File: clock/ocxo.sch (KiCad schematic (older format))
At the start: 32 parts

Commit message: Fill in some of the BOM entries.
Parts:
- removed Q?: Q_NPN_BCE, symbol Q_NPN_BCE
- added C?: 470pF, symbol C
- added Q?: MMBT3904, symbol Q_NPN_BEC
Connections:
- wire segments 164 -> 127
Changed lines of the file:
@@
 $Descr A4 11693 8268
 encoding utf-8
-Sheet 3 5
+Sheet 2 5
 Title ""
 Date ""
@@
 $EndComp
 $Comp
-L Q_NPN_BCE Q?
-U 1 1 561CA517
-P 6050 2650
-F 0 "Q?" H 6350 2700 50  0000 R CNN
-F 1 "Q_NPN_BCE" H 6650 2600 50  0000 R CNN
-F 2 "" H 6250 2750 29  0000 C CNN
-F 3 "" H 6050 2650 60  0000 C CNN
-	1    6050 2650
-	1    0    0    -1
-$EndComp
-$Comp
 L R_local R?
 U 1 1 561CA9D0
@@
 	1650 1350 7100 1350
 Wire Wire Line
-	4950 1150 5150 1150
-Wire Wire Line
-	5150 1150 6600 1150
-Wire Wire Line
-	6600 1150 6950 1150
-Wire Wire Line
-	6950 1150 7100 1150
+	4950 1150 7100 1150
 Wire Wire Line
 	6950 1450 6950 1150
@@
 	6600 1750 6600 1950
 Wire Wire Line
-	6600 1950 6950 1950
-Wire Wire Line
-	6950 1950 7350 1950
-Wire Wire Line
-	7350 1950 7700 1950
-Wire Wire Line
-	7700 1950 8550 1950
-Wire Wire Line
-	8550 1950 8950 1950
+	6600 1950 8950 1950
 Wire Wire Line
 	6950 1950 6950 1750
@@
 	4450 1150 4650 1150
 Wire Wire Line
-	1650 1150 2850 1150
-Wire Wire Line
-	2850 1150 3900 1150
-Wire Wire Line
-	3900 1150 4150 1150
-Wire Wire Line
-	3900 1150 3900 1550
-Wire Wire Line
-	3900 1550 3900 1650
+	1650 1150 4150 1150
+Wire Wire Line
+	3900 1150 3900 1650
 Wire Wire Line
 	3900 1550 4750 1550
 Wire Wire Line
-	4750 1550 4750 1750
-Wire Wire Line
-	4750 1750 4750 1900
+	4750 1550 4750 1900
 Connection ~ 3900 1150
 Wire Wire Line
@@
 	7700 1950 7700 1650
 Wire Wire Line
-	8300 1150 8550 1150
-Wire Wire Line
-	8550 1150 8950 1150
-Wire Wire Line
-	8950 1150 9350 1150
+	8300 1150 9350 1150
 Wire Wire Line
 	8550 1450 8550 1150
@@
 	1650 1550 2250 1550
 Wire Wire Line
-	2250 1550 2250 1750
-Wire Wire Line
-	2250 1750 2250 2400
-Wire Wire Line
-	2850 1150 2850 1750
-Wire Wire Line
-	2850 1750 2850 1850
-Wire Wire Line
-	2850 1850 2850 2400
+	2250 1550 2250 2400
+Wire Wire Line
+	2850 1150 2850 2400
 Connection ~ 2850 1150
 Wire Wire Line
@@
 	2550 2350 1950 2350
 Wire Wire Line
-	1950 2150 1950 2350
-Wire Wire Line
-	1950 2350 1950 2500
+	1950 2150 1950 2500
 Connection ~ 1950 2350
 Wire Wire Line
@@
 	4250 2600 4050 2600
 Wire Wire Line
-	4050 2600 4050 2700
-Wire Wire Line
-	4050 2700 4050 3200
-Wire Wire Line
-	4050 3200 4050 3300
+	4050 2600 4050 3300
 Wire Wire Line
 	4250 2700 4050 2700
@@
 	2550 3600 2550 3700
 Wire Wire Line
-	5150 6500 5250 6500
-Wire Wire Line
-	5250 6500 5600 6500
-Wire Wire Line
-	5600 6500 5900 6500
+	5150 6500 5900 6500
 Wire Wire Line
 	5250 6500 5250 6150
@@
 	4350 6400 4450 6400
 Wire Wire Line
-	4000 6400 4000 6500
-Wire Wire Line
-	4000 6500 4000 6600
-Wire Wire Line
-	4000 6600 4000 6700
+	4000 6400 4000 6700
 Wire Wire Line
 	4450 6600 4000 6600
@@
 	3550 7000 3550 7150
 Wire Wire Line
-	3100 7150 3550 7150
-Wire Wire Line
-	3550 7150 4000 7150
-Wire Wire Line
-	4000 7150 4750 7150
-Wire Wire Line
-	4750 7150 5900 7150
+	3100 7150 5900 7150
 Wire Wire Line
 	4750 6800 4750 7150
@@
 	4000 6100 4000 6000
 Wire Wire Line
-	3100 6000 4000 6000
-Wire Wire Line
-	4000 6000 4750 6000
+	3100 6000 4750 6000
 Wire Wire Line
 	4750 6000 4750 6200
@@
 Connection ~ 3550 7150
 Wire Wire Line
-	3100 5900 3100 6000
-Wire Wire Line
-	3100 6000 3100 6700
+	3100 5900 3100 6700
 Connection ~ 4000 6000
 Wire Wire Line
@@
 	5600 6050 5600 5900
 Wire Wire Line
-	5600 5300 5600 5500
-Wire Wire Line
-	5600 5500 5600 5600
+	5600 5300 5600 5600
 Wire Wire Line
 	5200 4900 5600 4900
@@
 	7050 5050 7050 5400
 Wire Wire Line
-	7050 5400 6950 5400
-Wire Wire Line
-	7050 5400 7300 5400
-Wire Wire Line
-	7300 5400 7500 5400
-Wire Wire Line
-	5600 5500 5900 5500
-Wire Wire Line
-	5900 5500 6250 5500
+	6950 5400 7500 5400
+Wire Wire Line
+	5600 5500 6250 5500
 Connection ~ 5600 5500
 Wire Wire Line
-	5900 6350 5900 6500
-Wire Wire Line
-	5900 6500 5900 6600
+	5900 6350 5900 6600
 Connection ~ 5600 6500
 Wire Wire Line
@@
 Connection ~ 5900 6500
 Wire Wire Line
-	5900 6900 5900 7150
-Wire Wire Line
-	5900 7150 5900 7250
+	5900 6900 5900 7250
 Connection ~ 5900 7150
 Connection ~ 7050 5400
@@
 	6550 5700 6550 5800
 Wire Wire Line
-	4700 5300 4700 5400
-Wire Wire Line
-	4700 5400 4700 5500
+	4700 5300 4700 5500
 Wire Wire Line
 	4700 5400 4500 5400
@@
 	7300 3850 7300 3650
 Wire Wire Line
-	8300 5400 8600 5400
-Wire Wire Line
-	8600 5400 10100 5400
+	8300 5400 10100 5400
 Wire Wire Line
 	8400 3950 8600 3950
@@
 	4500 4400 4700 4400
 Wire Wire Line
-	4700 4200 4700 4400
-Wire Wire Line
-	4700 4400 4700 4500
+	4700 4200 4700 4500
 Connection ~ 4700 4400
 Wire Wire Line
@@
 	7300 3250 7900 3250
 Wire Wire Line
-	7900 3150 7900 3250
-Wire Wire Line
-	7900 3250 7900 3550
+	7900 3150 7900 3550
 Wire Wire Line
 	7900 5000 7900 4900
@@
 	9000 4600 9000 4500
 Wire Wire Line
-	5450 2300 5750 2300
-Wire Wire Line
-	5750 2300 6150 2300
-Wire Wire Line
-	6150 2300 6150 2450
-Wire Wire Line
-	5850 2650 5750 2650
-Wire Wire Line
-	5750 2650 5750 2300
-Connection ~ 5750 2300
-Wire Wire Line
-	6150 2850 6150 2950
-Wire Wire Line
-	6150 2950 5550 2950
+	5450 2300 6400 2300
+Wire Wire Line
+	6400 2300 6400 2450
+Wire Wire Line
+	6100 2650 6000 2650
+Wire Wire Line
+	6000 2650 6000 2300
+Connection ~ 6000 2300
+Wire Wire Line
+	6400 2850 6400 2950
+Wire Wire Line
+	6400 2950 5550 2950
 Wire Wire Line
 	5550 2950 5550 2700
@@
 Wire Wire Line
 	6550 5100 6550 5000
+$Comp
+L Q_NPN_BEC Q?
+U 1 1 562FC26B
+P 6300 2650
+F 0 "Q?" H 6600 2700 50  0000 R CNN
+F 1 "MMBT3904" H 6900 2600 50  0000 R CNN
+F 2 "" H 6500 2750 29  0000 C CNN
+F 3 "" H 6300 2650 60  0000 C CNN
+F 4 "MMBT3904" H 6700 2500 50  0001 C CNN "PartNum"
+	1    6300 2650
+	1    0    0    -1
+$EndComp
+$Comp
+L C C?
+U 1 1 563107A4
+P 5750 2600
+F 0 "C?" H 5775 2700 50  0000 L CNN
+F 1 "470pF" H 5775 2500 50  0000 L CNN
+F 2 "" H 5788 2450 30  0000 C CNN
+F 3 "" H 5750 2600 60  0000 C CNN
+	1    5750 2600
+	1    0    0    -1
+$EndComp
+Wire Wire Line
+	5750 2300 5750 2450
+Connection ~ 5750 2300
+Wire Wire Line
+	5750 2750 5750 2950
+Connection ~ 5750 2950
 $EndSCHEMATC

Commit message: Update parts with parameter detail and BOM information.
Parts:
- removed C? (x12): 0.1uF, symbol C
- removed C?: 10uF, symbol C
- removed C?: 22uF, symbol C
- removed R? (x2): 0.05, symbol R_local
- removed R? (x7): 100K, symbol R_local
- removed U?: LTC2990, symbol LTC2990
- removed U?: cx210, symbol cx210
- removed U?: PCA9306, symbol PCA9306
- removed U?: LP3853, symbol LP3853
- removed U?: FVXO-HC53, symbol FVXO-HC53
- removed U?: DAC8830, symbol DAC8830
- removed U? (x2): LVM722, symbol LVM722
- added C?: 10uF, Capacitors_SMD:C_1206_HandSoldering, symbol C
- added C? (x12): 0.1uF, Capacitors_SMD:C_0805_HandSoldering, symbol C
- added C?: 22uF, Capacitors_SMD:C_1206_HandSoldering, symbol C
- added R?: 0.1R, symbol R_CSM2512
- added R? (x5): 100K, Resistors_SMD:R_0805_HandSoldering, symbol R_local
- added R? (x2): 10K, Resistors_SMD:R_0805_HandSoldering, symbol R_local
- added U?: LP3853, symbol LP3853
- added U?: PCA9306, symbol PCA9306
- added U?: LTC2990, symbol LTC2990
- added U?: DAC8830, symbol DAC8830
- added U?: FVXO-HC53, symbol FVXO-HC53
- added U?: cx210, symbol cx210
- added U? (x2): LMV722, symbol LMV722
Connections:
- wire segments 127 -> 166

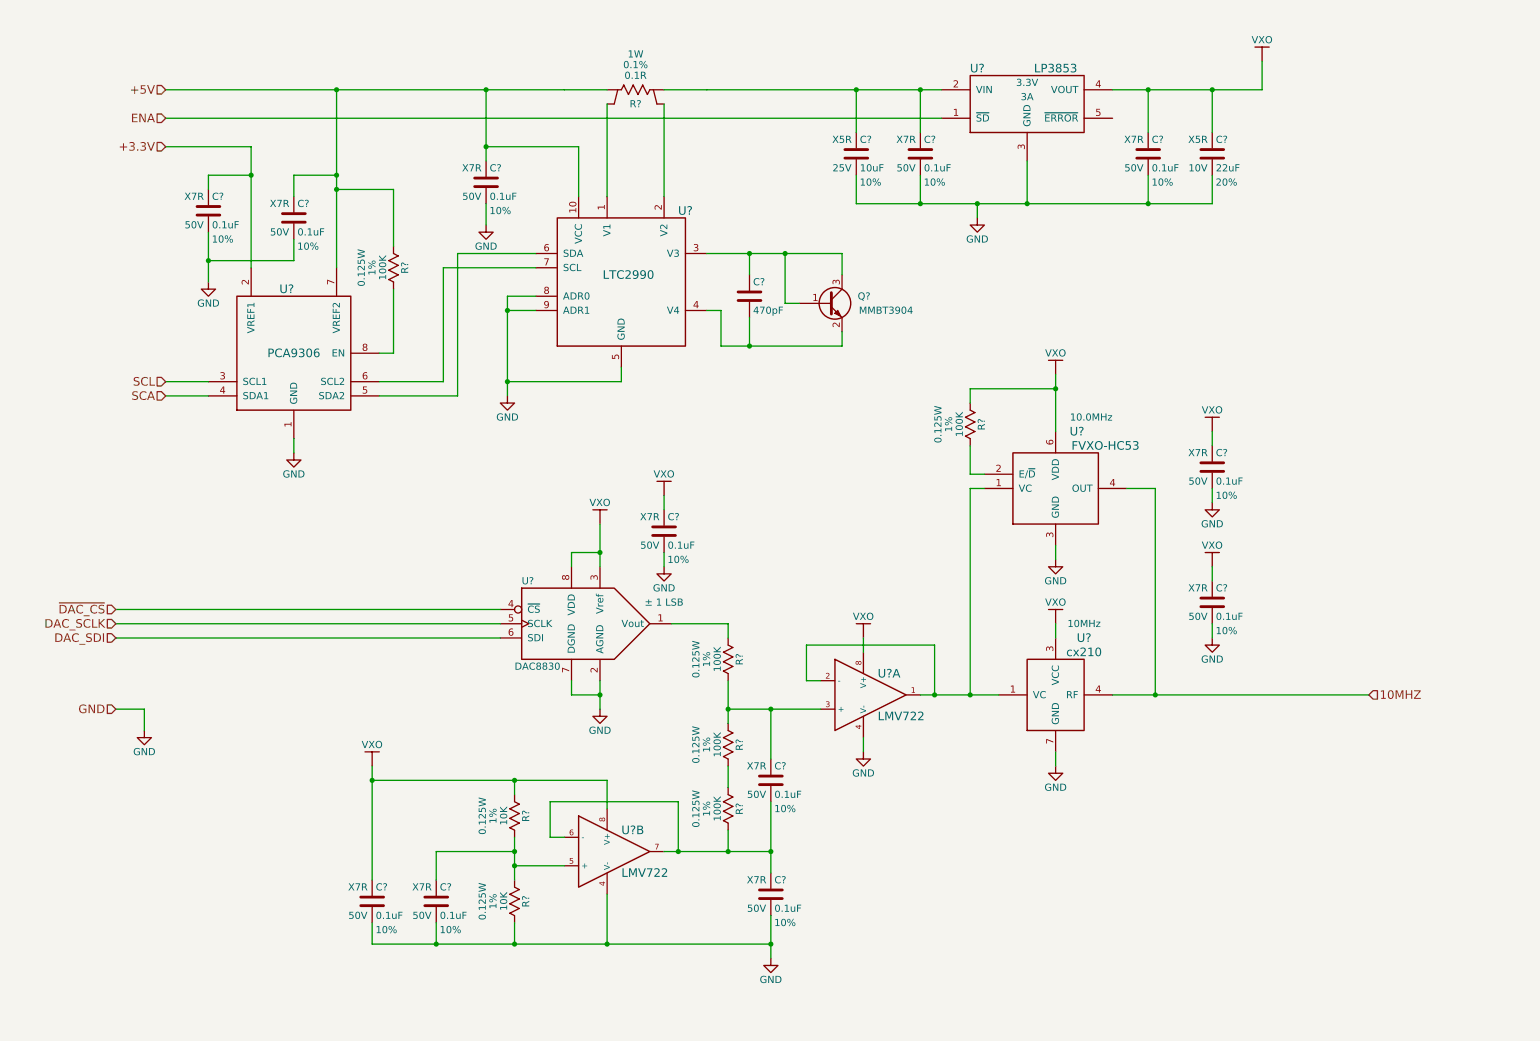
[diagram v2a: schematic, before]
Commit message: Add parameter for RF connector. Start adding display connections.
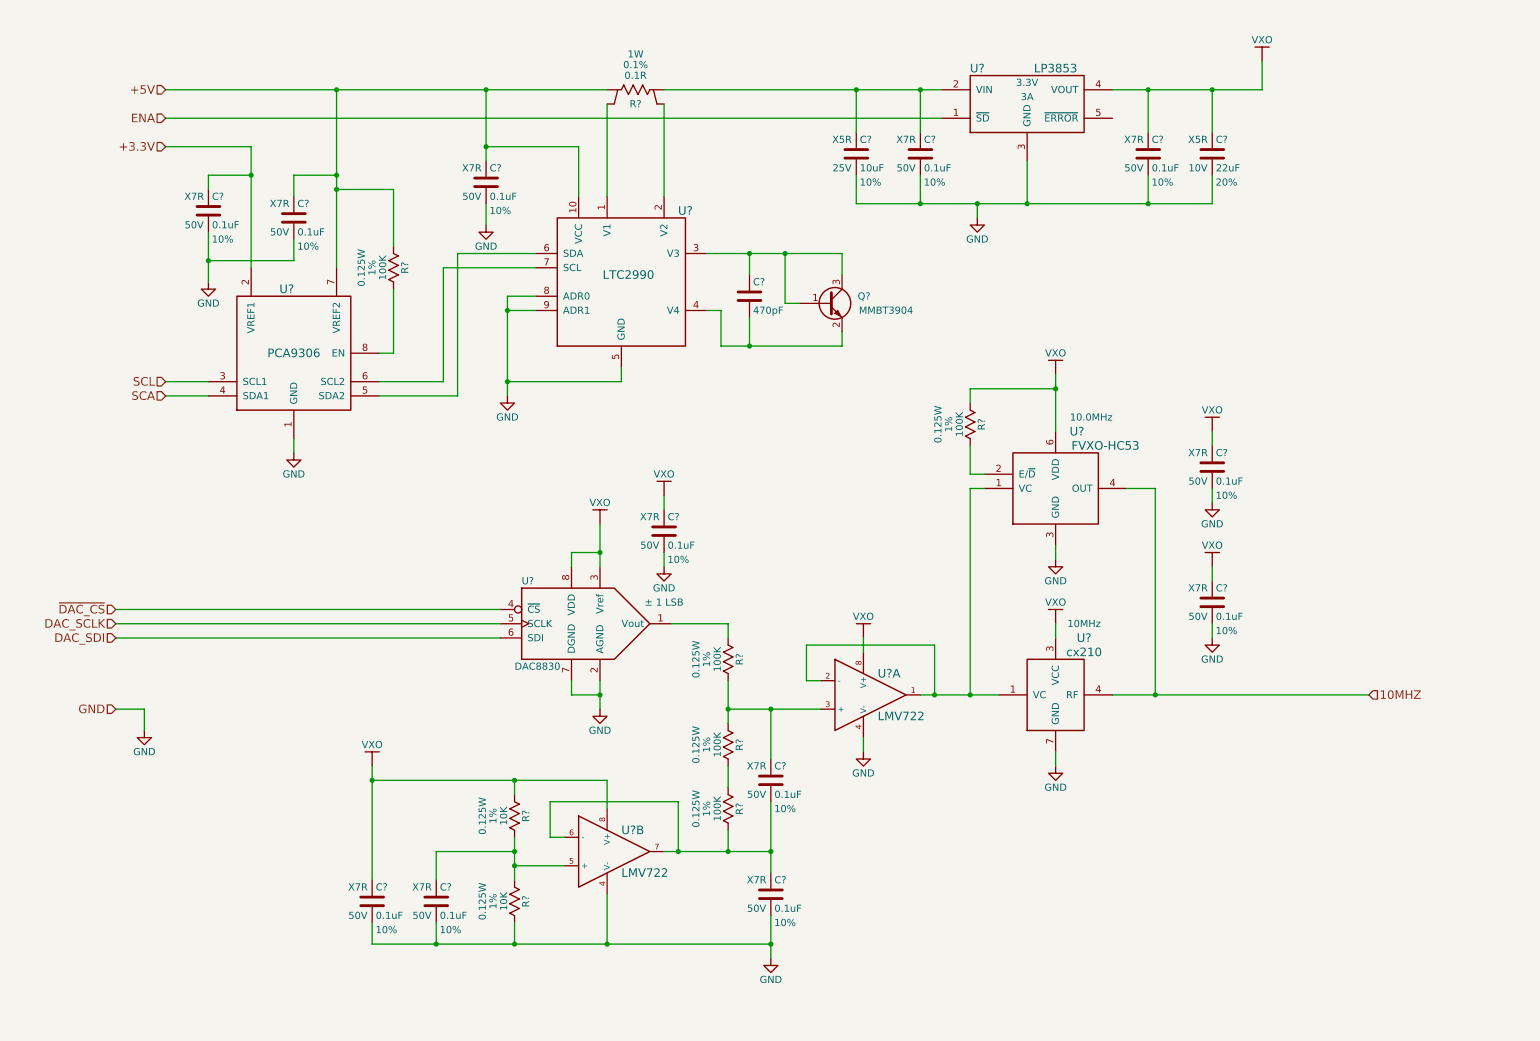
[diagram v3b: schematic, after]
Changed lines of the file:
@@
 	1650 1350 7100 1350
 Wire Wire Line
-	5150 1150 5450 1150
-Wire Wire Line
-	5450 1150 6500 1150
-Wire Wire Line
-	6500 1150 6950 1150
-Wire Wire Line
-	6950 1150 7100 1150
+	5150 1150 7100 1150
 Wire Wire Line
 	6950 1450 6950 1150
@@
 	6500 1750 6500 1950
 Wire Wire Line
-	6500 1950 6950 1950
-Wire Wire Line
-	6950 1950 7350 1950
-Wire Wire Line
-	7350 1950 7700 1950
-Wire Wire Line
-	7700 1950 8550 1950
-Wire Wire Line
-	8550 1950 9000 1950
+	6500 1950 9000 1950
 Wire Wire Line
 	6950 1950 6950 1750
@@
 	5150 1900 5150 1250
 Wire Wire Line
-	1650 1150 2850 1150
-Wire Wire Line
-	2850 1150 3900 1150
-Wire Wire Line
-	3900 1150 4450 1150
-Wire Wire Line
-	4450 1150 4750 1150
-Wire Wire Line
-	3900 1150 3900 1550
-Wire Wire Line
-	3900 1550 3900 1650
+	1650 1150 4750 1150
+Wire Wire Line
+	3900 1150 3900 1650
 Wire Wire Line
 	3900 1550 4550 1550
@@
 	7700 1950 7700 1650
 Wire Wire Line
-	8300 1150 8550 1150
-Wire Wire Line
-	8550 1150 9000 1150
-Wire Wire Line
-	9000 1150 9350 1150
+	8300 1150 9350 1150
 Wire Wire Line
 	8550 1450 8550 1150
@@
 	1650 1550 2250 1550
 Wire Wire Line
-	2250 1550 2250 1750
-Wire Wire Line
-	2250 1750 2250 2400
-Wire Wire Line
-	2850 1150 2850 1750
-Wire Wire Line
-	2850 1750 2850 1850
-Wire Wire Line
-	2850 1850 2850 2400
+	2250 1550 2250 2400
+Wire Wire Line
+	2850 1150 2850 2400
 Connection ~ 2850 1150
 Wire Wire Line
@@
 	2550 2350 1950 2350
 Wire Wire Line
-	1950 2150 1950 2350
-Wire Wire Line
-	1950 2350 1950 2500
+	1950 2150 1950 2500
 Connection ~ 1950 2350
 Wire Wire Line
@@
 	4250 2600 4050 2600
 Wire Wire Line
-	4050 2600 4050 2700
-Wire Wire Line
-	4050 2700 4050 3200
-Wire Wire Line
-	4050 3200 4050 3300
+	4050 2600 4050 3300
 Wire Wire Line
 	4250 2700 4050 2700
@@
 	2550 3600 2550 3700
 Wire Wire Line
-	5150 6500 5250 6500
-Wire Wire Line
-	5250 6500 5600 6500
-Wire Wire Line
-	5600 6500 5900 6500
+	5150 6500 5900 6500
 Wire Wire Line
 	5250 6500 5250 6150
@@
 	4350 6400 4450 6400
 Wire Wire Line
-	4100 6400 4100 6500
-Wire Wire Line
-	4100 6500 4100 6600
-Wire Wire Line
-	4100 6600 4100 6700
+	4100 6400 4100 6700
 Wire Wire Line
 	4450 6600 4100 6600
@@
 	3550 7000 3550 7150
 Wire Wire Line
-	3100 7150 3550 7150
-Wire Wire Line
-	3550 7150 4100 7150
-Wire Wire Line
-	4100 7150 4750 7150
-Wire Wire Line
-	4750 7150 5900 7150
+	3100 7150 5900 7150
 Wire Wire Line
 	4750 6800 4750 7150
@@
 	4100 6100 4100 6000
 Wire Wire Line
-	3100 6000 4100 6000
-Wire Wire Line
-	4100 6000 4750 6000
+	3100 6000 4750 6000
 Wire Wire Line
 	4750 6000 4750 6200
@@
 Connection ~ 3550 7150
 Wire Wire Line
-	3100 5900 3100 6000
-Wire Wire Line
-	3100 6000 3100 6700
+	3100 5900 3100 6700
 Connection ~ 4100 6000
 Wire Wire Line
@@
 	5600 6050 5600 5900
 Wire Wire Line
-	5600 5300 5600 5500
-Wire Wire Line
-	5600 5500 5600 5600
+	5600 5300 5600 5600
 Wire Wire Line
 	5200 4900 5600 4900
@@
 	7050 5050 7050 5400
 Wire Wire Line
-	6950 5400 7050 5400
-Wire Wire Line
-	7050 5400 7300 5400
-Wire Wire Line
-	7300 5400 7500 5400
-Wire Wire Line
-	5600 5500 5900 5500
-Wire Wire Line
-	5900 5500 6250 5500
+	6950 5400 7500 5400
+Wire Wire Line
+	5600 5500 6250 5500
 Connection ~ 5600 5500
 Wire Wire Line
-	5900 6150 5900 6500
-Wire Wire Line
-	5900 6500 5900 6650
+	5900 6150 5900 6650
 Connection ~ 5600 6500
 Wire Wire Line
@@
 Connection ~ 5900 6500
 Wire Wire Line
-	5900 6950 5900 7150
-Wire Wire Line
-	5900 7150 5900 7250
+	5900 6950 5900 7250
 Connection ~ 5900 7150
 Connection ~ 7050 5400
@@
 	6550 5700 6550 5800
 Wire Wire Line
-	4700 5300 4700 5400
-Wire Wire Line
-	4700 5400 4700 5500
+	4700 5300 4700 5500
 Wire Wire Line
 	4700 5400 4500 5400
@@
 	7300 3850 7300 3650
 Wire Wire Line
-	8300 5400 8600 5400
-Wire Wire Line
-	8600 5400 10100 5400
+	8300 5400 10100 5400
 Wire Wire Line
 	8400 3950 8600 3950
@@
 	4500 4400 4700 4400
 Wire Wire Line
-	4700 4200 4700 4400
-Wire Wire Line
-	4700 4400 4700 4500
+	4700 4200 4700 4500
 Connection ~ 4700 4400
 Wire Wire Line
@@
 	7300 3250 7900 3250
 Wire Wire Line
-	7900 3150 7900 3250
-Wire Wire Line
-	7900 3250 7900 3550
+	7900 3150 7900 3550
 Wire Wire Line
 	7900 5000 7900 4900
@@
 	9000 4600 9000 4500
 Wire Wire Line
-	5450 2300 5750 2300
-Wire Wire Line
-	5750 2300 6000 2300
-Wire Wire Line
-	6000 2300 6400 2300
+	5450 2300 6400 2300
 Wire Wire Line
 	6400 2300 6400 2450
@@
 	6400 2950 6400 2850
 Wire Wire Line
-	5550 2950 5750 2950
-Wire Wire Line
-	5750 2950 6400 2950
+	5550 2950 6400 2950
 Wire Wire Line
 	5550 2950 5550 2700

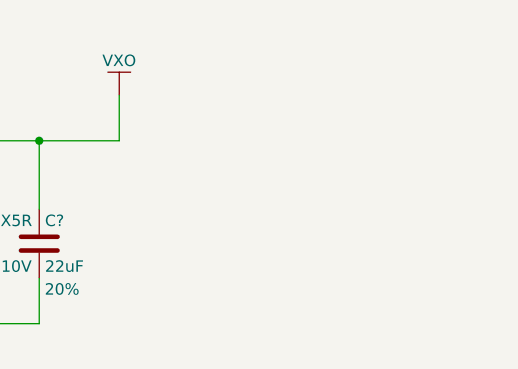
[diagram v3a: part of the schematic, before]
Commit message: Add sheet for RTC and temperature sensors.
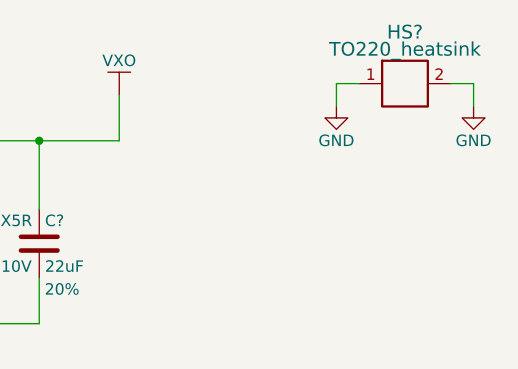
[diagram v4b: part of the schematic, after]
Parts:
- added HS?: TO220_heatsink, symbol TO220_heatsink
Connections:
- net GND: now also HS?.1, HS?.2
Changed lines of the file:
@@
 $Descr A4 11693 8268
 encoding utf-8
-Sheet 2 5
+Sheet 2 6
 Title ""
 Date ""
@@
 	0    1    1    0
 $EndComp
+$Comp
+L TO220_heatsink HS?
+U 1 1 563564D2
+P 10600 900
+F 0 "HS?" H 10600 1125 60  0000 C CNN
+F 1 "TO220_heatsink" H 10600 1050 60  0000 C CNN
+F 2 "" H 10600 900 60  0000 C CNN
+F 3 "" H 10600 900 60  0000 C CNN
+F 4 "Aavid" H 10600 1325 60  0001 C CNN "Manufacturer"
+F 5 "581002B02500G" H 10600 1225 60  0001 C CNN "PartNum"
+	1    10600 900
+	1    0    0    -1
+$EndComp
+$Comp
+L GND #PWR?
+U 1 1 56356688
+P 10300 1000
+F 0 "#PWR?" H 10300 750 50  0001 C CNN
+F 1 "GND" H 10300 850 50  0000 C CNN
+F 2 "" H 10300 1000 60  0000 C CNN
+F 3 "" H 10300 1000 60  0000 C CNN
+	1    10300 1000
+	1    0    0    -1
+$EndComp
+$Comp
+L GND #PWR?
+U 1 1 563568AD
+P 10900 1000
+F 0 "#PWR?" H 10900 750 50  0001 C CNN
+F 1 "GND" H 10900 850 50  0000 C CNN
+F 2 "" H 10900 1000 60  0000 C CNN
+F 3 "" H 10900 1000 60  0000 C CNN
+	1    10900 1000
+	1    0    0    -1
+$EndComp
+Wire Wire Line
+	10800 900  10900 900
+Wire Wire Line
+	10900 900  10900 1000
+Wire Wire Line
+	10400 900  10300 900
+Wire Wire Line
+	10300 900  10300 1000
 $EndSCHEMATC
